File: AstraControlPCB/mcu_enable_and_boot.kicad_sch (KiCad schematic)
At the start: 12 parts, among them SW1 TS_Basic_Small, SW2 TS_Basic_Small

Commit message: Update wks file
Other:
- company: (none) -> LiveAstra Technologies
- title: MCU Enable and Boot -> AstraControl - Root
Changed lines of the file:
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@@
 	(paper "A4")
 	(title_block
-		(title "MCU Enable and Boot")
+		(title "AstraControl - Root")
+		(date "2024-08-26")
+		(rev "A")
+		(company "LiveAstra Technologies")
 	)
 	(junction
@@
 		(effects
 			(font
-				(face "Sarabun")
+				(face "ING Me")
 				(size 3 3)
 				(color 255 255 255 1)
@@
 		(effects
 			(font
-				(face "Sarabun")
+				(face "ING Me")
 				(size 1.5 1.5)
 				(color 255 255 255 1)

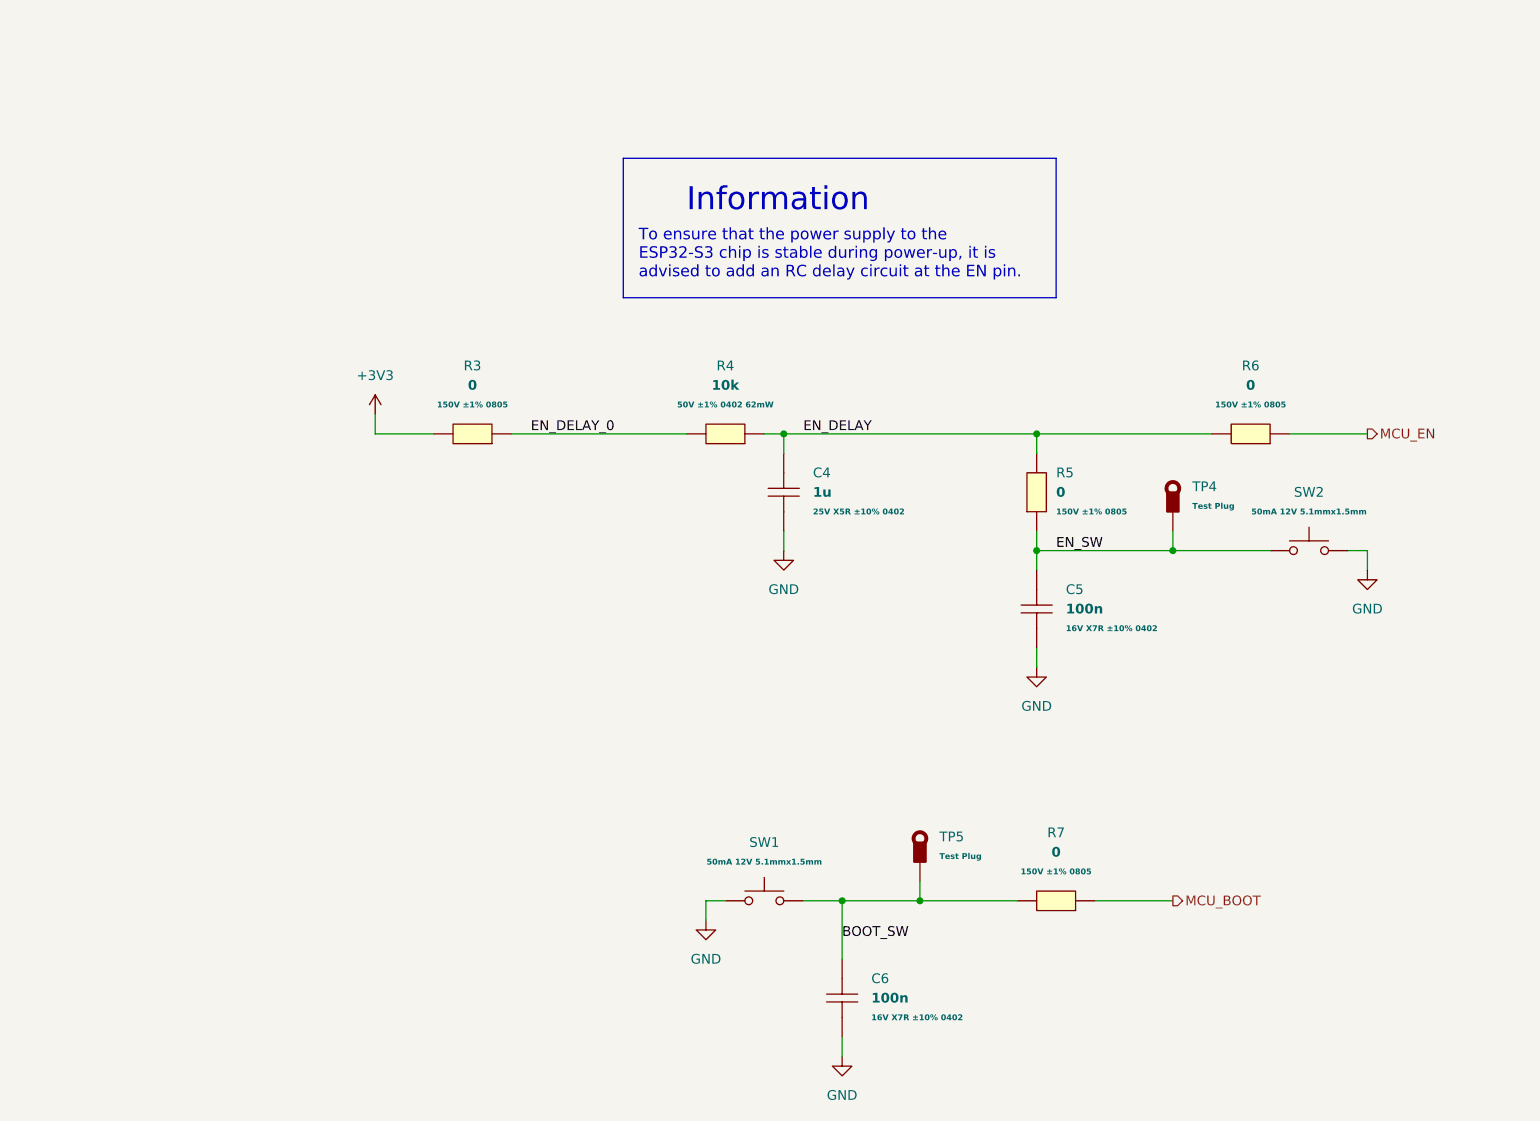
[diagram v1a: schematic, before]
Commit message: Remove plus minus symbol
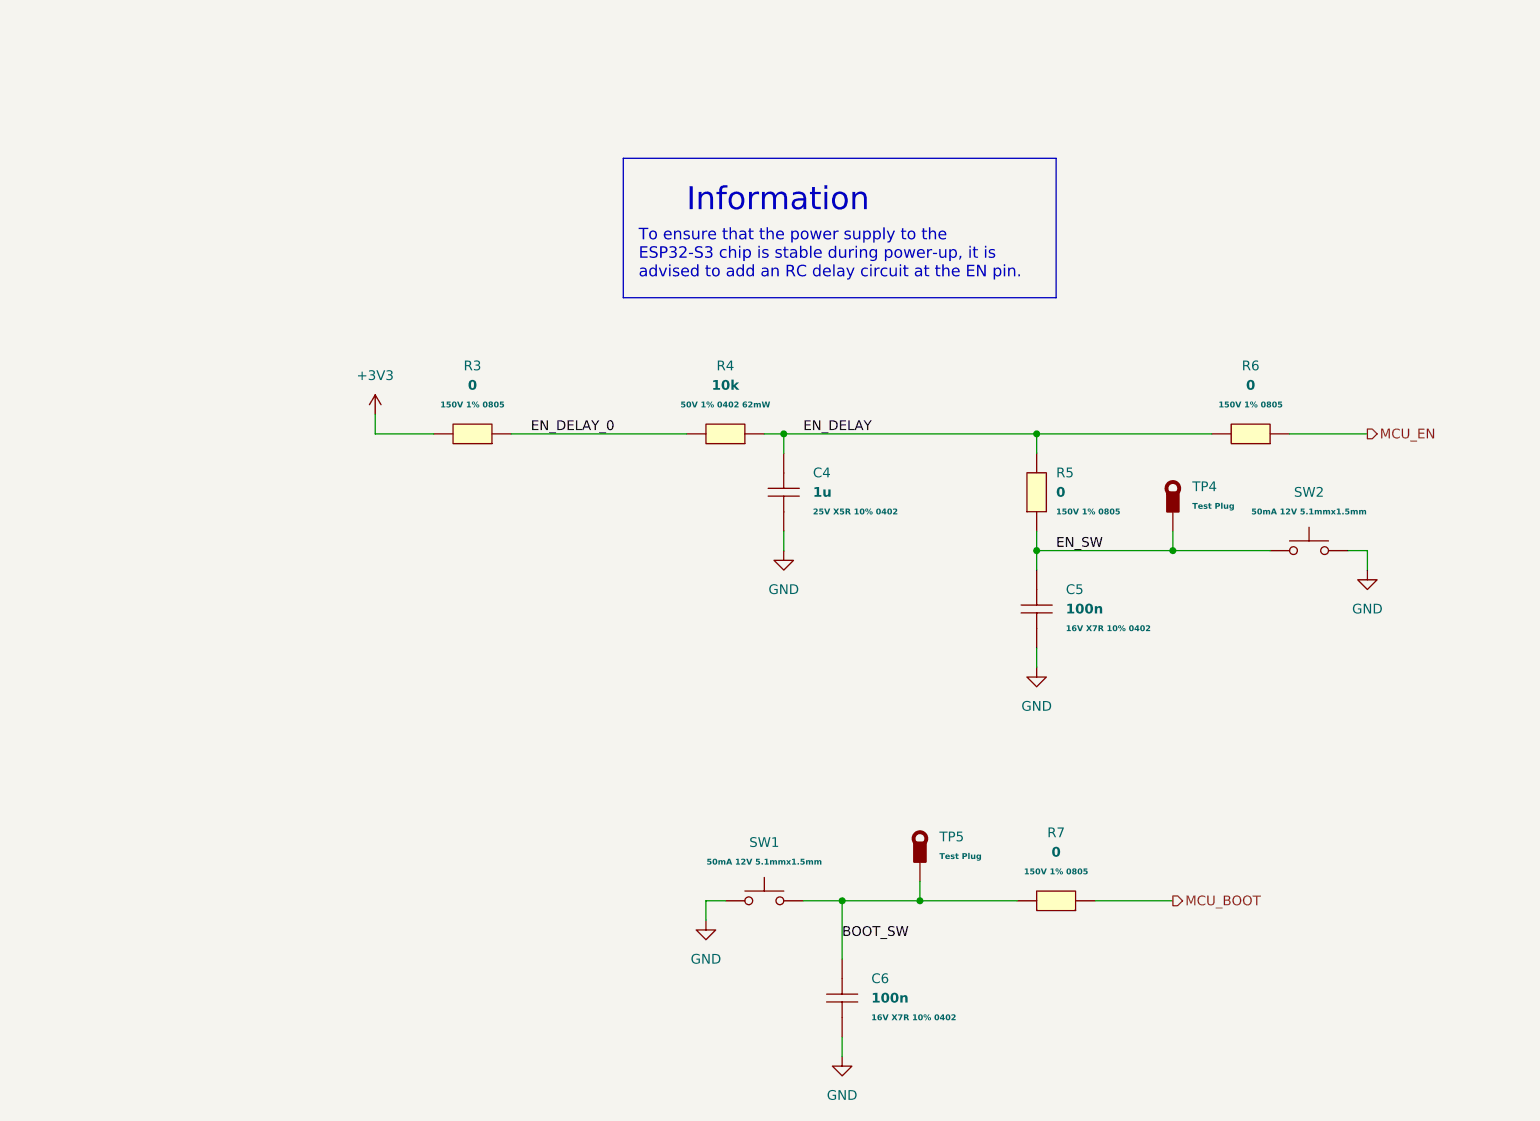
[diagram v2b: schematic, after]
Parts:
- C4: Extra Values 25V X5R ±10% 0402 -> 25V X5R 10% 0402
- C5, C6: Extra Values 16V X7R ±10% 0402 -> 16V X7R 10% 0402
- R3, R5, R6, R7: Extra Values 150V ±1% 0805 -> 150V 1% 0805
- R4: Extra Values 50V ±1% 0402 62mW -> 50V 1% 0402 62mW
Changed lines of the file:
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@@
 			)
 		)
-		(property "Extra Values" "16V X7R ±10% 0402"
+		(property "Extra Values" "16V X7R 10% 0402"
 			(at 156.21 101.5999 90)
 			(effects
@@
 				)
 				(justify right)
-			)
-		)
-		(property "Extra Value" ""
-			(at 152.4 99.06 0)
-			(effects
-				(font
-					(size 1.27 1.27)
-				)
-				(hide yes)
 			)
 		)
@@
 		(dnp no)
 		(fields_autoplaced yes)
-		(property "Reference" "#PWR014"
+		(property "Reference" "#PWR14"
 			(at 152.4 113.03 0)
 			(effects
@@
 			(project "AstraControl"
 				(path "/9a751838-dce8-4d69-8a02-736625ac74e7/0db21d8e-3390-4d67-877f-0e5d98e37848/d7820a84-5a43-4050-a708-637b006ce625"
-					(reference "#PWR014")
+					(reference "#PWR14")
 					(unit 1)
 				)
@@
 			)
 		)
-		(property "Extra Values" "150V ±1% 0805"
+		(property "Extra Values" "150V 1% 0805"
 			(at 154.94 86.3599 90)
 			(effects
@@
 				)
 				(justify right)
-			)
-		)
-		(property "Extra Value" ""
-			(at 152.4 83.82 0)
-			(effects
-				(font
-					(size 1.27 1.27)
-				)
-				(hide yes)
 			)
 		)
@@
 		(dnp no)
 		(fields_autoplaced yes)
-		(property "Reference" "#PWR011"
+		(property "Reference" "#PWR11"
 			(at 66.04 77.47 0)
 			(effects
@@
 			(project "AstraControl"
 				(path "/9a751838-dce8-4d69-8a02-736625ac74e7/0db21d8e-3390-4d67-877f-0e5d98e37848/d7820a84-5a43-4050-a708-637b006ce625"
-					(reference "#PWR011")
+					(reference "#PWR11")
 					(unit 1)
 				)
@@
 			)
 		)
-		(property "Extra Values" "50V ±1% 0402 62mW"
+		(property "Extra Values" "50V 1% 0402 62mW"
 			(at 111.76 72.39 0)
 			(effects
@@
 					(bold yes)
 				)
-			)
-		)
-		(property "Extra Value" ""
-			(at 111.76 76.2 0)
-			(effects
-				(font
-					(size 1.27 1.27)
-				)
-				(hide yes)
 			)
 		)
@@
 		(dnp no)
 		(fields_autoplaced yes)
-		(property "Reference" "#PWR015"
+		(property "Reference" "#PWR15"
 			(at 127 163.83 0)
 			(effects
@@
 			(project "AstraControl"
 				(path "/9a751838-dce8-4d69-8a02-736625ac74e7/0db21d8e-3390-4d67-877f-0e5d98e37848/d7820a84-5a43-4050-a708-637b006ce625"
-					(reference "#PWR015")
+					(reference "#PWR15")
 					(unit 1)
 				)
@@
 			)
 		)
-		(property "Extra Values" "150V ±1% 0805"
+		(property "Extra Values" "150V 1% 0805"
 			(at 180.34 72.39 0)
 			(effects
@@
 					(bold yes)
 				)
-			)
-		)
-		(property "Extra Value" ""
-			(at 180.34 76.2 0)
-			(effects
-				(font
-					(size 1.27 1.27)
-				)
-				(hide yes)
 			)
 		)
@@
 			)
 		)
-		(property "Extra Value" ""
-			(at 170.18 88.9 0)
-			(effects
-				(font
-					(size 1.27 1.27)
-				)
-				(hide yes)
-			)
-		)
 		(pin "1"
 		)
@@
 		(dnp no)
 		(fields_autoplaced yes)
-		(property "Reference" "#PWR016"
+		(property "Reference" "#PWR16"
 			(at 195.58 100.33 0)
 			(effects
@@
 			(project "AstraControl"
 				(path "/9a751838-dce8-4d69-8a02-736625ac74e7/0db21d8e-3390-4d67-877f-0e5d98e37848/d7820a84-5a43-4050-a708-637b006ce625"
-					(reference "#PWR016")
+					(reference "#PWR16")
 					(unit 1)
 				)
@@
 		(dnp no)
 		(fields_autoplaced yes)
-		(property "Reference" "#PWR013"
+		(property "Reference" "#PWR13"
 			(at 109.22 146.05 0)
 			(effects
@@
 			(project "AstraControl"
 				(path "/9a751838-dce8-4d69-8a02-736625ac74e7/0db21d8e-3390-4d67-877f-0e5d98e37848/d7820a84-5a43-4050-a708-637b006ce625"
-					(reference "#PWR013")
+					(reference "#PWR13")
 					(unit 1)
 				)
@@
 			)
 		)
-		(property "Extra Values" "150V ±1% 0805"
+		(property "Extra Values" "150V 1% 0805"
 			(at 78.74 72.39 0)
 			(effects
@@
 					(bold yes)
 				)
-			)
-		)
-		(property "Extra Value" ""
-			(at 78.74 76.2 0)
-			(effects
-				(font
-					(size 1.27 1.27)
-				)
-				(hide yes)
 			)
 		)
@@
 			)
 		)
-		(property "Extra Values" "150V ±1% 0805"
+		(property "Extra Values" "150V 1% 0805"
 			(at 154.94 133.35 0)
 			(effects
@@
 					(bold yes)
 				)
-			)
-		)
-		(property "Extra Value" ""
-			(at 154.94 137.16 0)
-			(effects
-				(font
-					(size 1.27 1.27)
-				)
-				(hide yes)
 			)
 		)
@@
 			)
 		)
-		(property "Extra Values" "16V X7R ±10% 0402"
+		(property "Extra Values" "16V X7R 10% 0402"
 			(at 130.81 152.3999 90)
 			(effects
@@
 				)
 				(justify left)
-			)
-		)
-		(property "Extra Value" ""
-			(at 127 149.86 0)
-			(effects
-				(font
-					(size 1.27 1.27)
-				)
-				(hide yes)
 			)
 		)
@@
 			)
 		)
-		(property "Extra Value" ""
-			(at 187.96 91.44 0)
-			(effects
-				(font
-					(size 1.27 1.27)
-				)
-				(hide yes)
-			)
-		)
 		(pin "2"
 		)
@@
 		(dnp no)
 		(fields_autoplaced yes)
-		(property "Reference" "#PWR012"
+		(property "Reference" "#PWR12"
 			(at 119.38 97.79 0)
 			(effects
@@
 			(project "AstraControl"
 				(path "/9a751838-dce8-4d69-8a02-736625ac74e7/0db21d8e-3390-4d67-877f-0e5d98e37848/d7820a84-5a43-4050-a708-637b006ce625"
-					(reference "#PWR012")
+					(reference "#PWR12")
 					(unit 1)
 				)
@@
 			)
 		)
-		(property "Extra Value" ""
-			(at 116.84 137.16 0)
-			(effects
-				(font
-					(size 1.27 1.27)
-				)
-				(hide yes)
-			)
-		)
 		(pin "2"
 		)
@@
 			)
 		)
-		(property "Extra Values" "25V X5R ±10% 0402"
+		(property "Extra Values" "25V X5R 10% 0402"
 			(at 123.19 86.3599 90)
 			(effects
@@
 				)
 				(justify left)
-			)
-		)
-		(property "Extra Value" ""
-			(at 119.38 83.82 0)
-			(effects
-				(font
-					(size 1.27 1.27)
-				)
-				(hide yes)
 			)
 		)
@@
 			)
 		)
-		(property "Extra Value" ""
-			(at 137.16 134.62 0)
-			(effects
-				(font
-					(size 1.27 1.27)
-				)
-				(hide yes)
-			)
-		)

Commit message: workflow
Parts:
- added INF2: ~, symbol LiveAstra:Information_Box
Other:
- note added: "MCU Enable & Boot"
- note removed: "Information"
- note removed: "To ensure that the power supply to the ESP32-S3 chip is stable during power-up, it is advised to add an RC delay circuit at the EN pin."
- moved on the sheet: C4, C5, C6, R3, R4, R5, R6, R7, SW1, SW2, TP4, TP5

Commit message: update
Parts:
- renumbered C6 to C5, C5 to C6, R7 to R6, R6 to R7, TP5 to TP3
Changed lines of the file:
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@@
 		(dnp no)
 		(fields_autoplaced yes)
-		(property "Reference" "C5"
+		(property "Reference" "C6"
 			(at 162.56 90.1699 90)
 			(effects
@@
 			(project "AstraControl"
 				(path "/9a751838-dce8-4d69-8a02-736625ac74e7/0db21d8e-3390-4d67-877f-0e5d98e37848/d7820a84-5a43-4050-a708-637b006ce625"
-					(reference "C5")
+					(reference "C6")
 					(unit 1)
 				)
@@
 		(dnp no)
 		(fields_autoplaced yes)
-		(property "Reference" "#PWR014"
+		(property "Reference" "#PWR015"
 			(at 158.75 106.68 0)
 			(effects
@@
 			(project "AstraControl"
 				(path "/9a751838-dce8-4d69-8a02-736625ac74e7/0db21d8e-3390-4d67-877f-0e5d98e37848/d7820a84-5a43-4050-a708-637b006ce625"
-					(reference "#PWR014")
+					(reference "#PWR015")
 					(unit 1)
 				)
@@
 		(dnp no)
 		(fields_autoplaced yes)
-		(property "Reference" "#PWR015"
+		(property "Reference" "#PWR014"
 			(at 133.35 157.48 0)
 			(effects
@@
 			(project "AstraControl"
 				(path "/9a751838-dce8-4d69-8a02-736625ac74e7/0db21d8e-3390-4d67-877f-0e5d98e37848/d7820a84-5a43-4050-a708-637b006ce625"
-					(reference "#PWR015")
+					(reference "#PWR014")
 					(unit 1)
 				)
@@
 		(dnp no)
 		(fields_autoplaced yes)
-		(property "Reference" "R6"
+		(property "Reference" "R7"
 			(at 186.69 60.96 0)
 			(effects
@@
 			(project "AstraControl"
 				(path "/9a751838-dce8-4d69-8a02-736625ac74e7/0db21d8e-3390-4d67-877f-0e5d98e37848/d7820a84-5a43-4050-a708-637b006ce625"
-					(reference "R6")
+					(reference "R7")
 					(unit 1)
 				)
@@
 		(dnp no)
 		(fields_autoplaced yes)
-		(property "Reference" "#PWR013"
+		(property "Reference" "#PWR012"
 			(at 115.57 139.7 0)
 			(effects
@@
 			(project "AstraControl"
 				(path "/9a751838-dce8-4d69-8a02-736625ac74e7/0db21d8e-3390-4d67-877f-0e5d98e37848/d7820a84-5a43-4050-a708-637b006ce625"
-					(reference "#PWR013")
+					(reference "#PWR012")
 					(unit 1)
 				)
@@
 		(dnp no)
 		(fields_autoplaced yes)
-		(property "Reference" "R7"
+		(property "Reference" "R6"
 			(at 161.29 121.92 0)
 			(effects
@@
 			(project "AstraControl"
 				(path "/9a751838-dce8-4d69-8a02-736625ac74e7/0db21d8e-3390-4d67-877f-0e5d98e37848/d7820a84-5a43-4050-a708-637b006ce625"
-					(reference "R7")
+					(reference "R6")
 					(unit 1)
 				)
@@
 		(dnp no)
 		(fields_autoplaced yes)
-		(property "Reference" "C6"
+		(property "Reference" "C5"
 			(at 137.16 140.9699 90)
 			(effects
@@
 			(project "AstraControl"
 				(path "/9a751838-dce8-4d69-8a02-736625ac74e7/0db21d8e-3390-4d67-877f-0e5d98e37848/d7820a84-5a43-4050-a708-637b006ce625"
-					(reference "C6")
+					(reference "C5")
 					(unit 1)
 				)
@@
 		(dnp no)
 		(fields_autoplaced yes)
-		(property "Reference" "#PWR012"
+		(property "Reference" "#PWR013"
 			(at 125.73 91.44 0)
 			(effects
@@
 			(project "AstraControl"
 				(path "/9a751838-dce8-4d69-8a02-736625ac74e7/0db21d8e-3390-4d67-877f-0e5d98e37848/d7820a84-5a43-4050-a708-637b006ce625"
-					(reference "#PWR012")
+					(reference "#PWR013")
 					(unit 1)
 				)
@@
 		(dnp no)
 		(fields_autoplaced yes)
-		(property "Reference" "TP5"
+		(property "Reference" "TP3"
 			(at 146.05 122.4576 0)
 			(effects
@@
 			(project "AstraControl"
 				(path "/9a751838-dce8-4d69-8a02-736625ac74e7/0db21d8e-3390-4d67-877f-0e5d98e37848/d7820a84-5a43-4050-a708-637b006ce625"
-					(reference "TP5")
-					(unit 1)
-				)
+					(reference "TP3")
+					(unit 1)
+				)

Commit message: update
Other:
- note added: "To ensure that the power supply to the ESP32-S3 chip is stable during power-up, it is advised to add an RC delay circuit at the EN pin."
- moved on the sheet: C4, C5, C6, R3, R4, R5, R6, R7, SW1, SW2, TP3, TP4

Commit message: Added MFN MPR to each components for eurocircuits
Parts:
- C4: MFN (none) -> Samsung Electro-Mechanics; MPR (none) -> CL05A105KA5NQNC
- C5, C6: MFN (none) -> Samsung Electro-Mechanics; MPN (none) -> CL05B104KO5NNNC
- R3, R5, R6, R7: MFN (none) -> UNI-ROYAL(Uniroyal Elec); MPN (none) -> 0805W8F0000T5E
- R4: MFN (none) -> UNI-ROYAL(Uniroyal Elec); MPN (none) -> 0402WGF1002TCE
- SW1, SW2: MFN (none) -> XKB Connection; MPN (none) -> TS-1187A-B-A-B
- TP3, TP4: MFN (none) -> ronghe; MPN (none) -> RH-5000

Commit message: Migrate library to submodule
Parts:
- C4: MPN (none) -> CL05A105KA5NQNC
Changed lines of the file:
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@@
+			)
+		)
+		(property "MPN" "CL05A105KA5NQNC"
+			(at 109.22 78.74 0)
+			(effects
+				(font
+					(size 1.27 1.27)
+				)
+				(hide yes)
 			)
 		)
